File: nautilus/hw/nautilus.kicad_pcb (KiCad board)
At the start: 4 copper layers, 54.7 x 55 mm, 120 parts, among them IC1 DRV8353SRTAR, IC2 STM32G474CEU6, IC3 MAX15062AATA+T, J1 XT30XT30PW_MALE, J2 Conn_01x02_Pin, J3 Conn_01x02_Pin, J4 Conn_01x02_Pin, M1 PAD24AWG_PAD, M2 PAD24AWG_PAD, M3 PAD24AWG_PAD, SW1 SW_Push, U2 CSD88599Q5DCT, U3 CSD88599Q5DCT, U4 AS5147, U5 CSD88599Q5DCT, U7 SN65HVD232

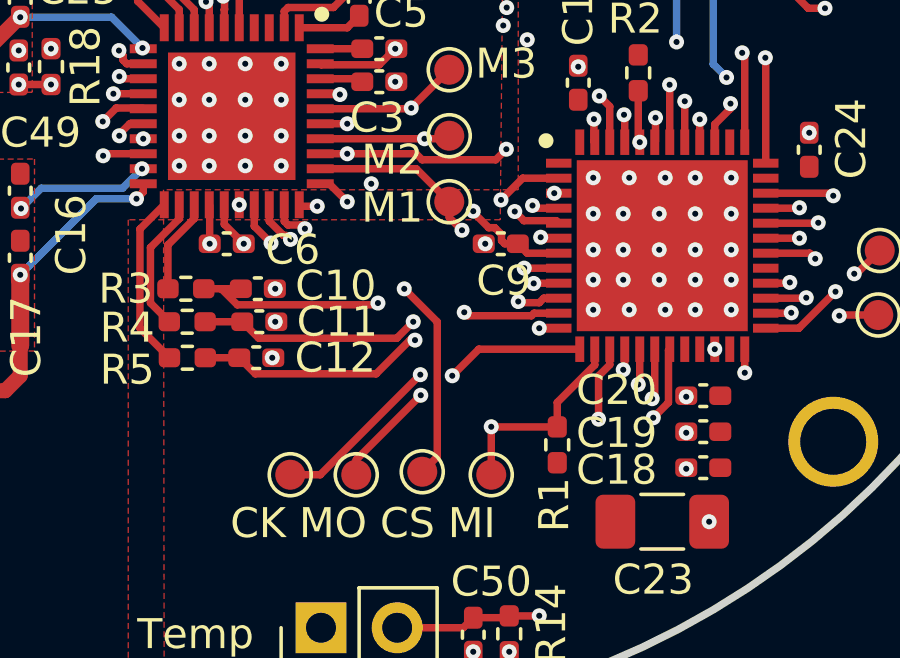
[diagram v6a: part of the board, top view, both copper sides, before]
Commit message: SPI: add temperature reading
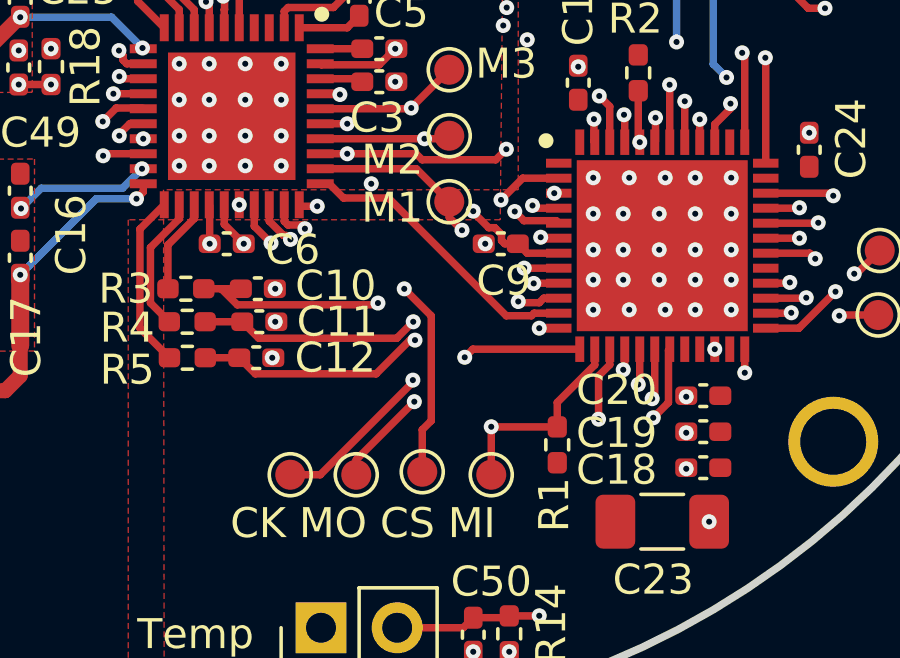
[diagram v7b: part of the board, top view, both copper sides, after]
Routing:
- net /MOTOR_ENABLE: vias 2 -> 0

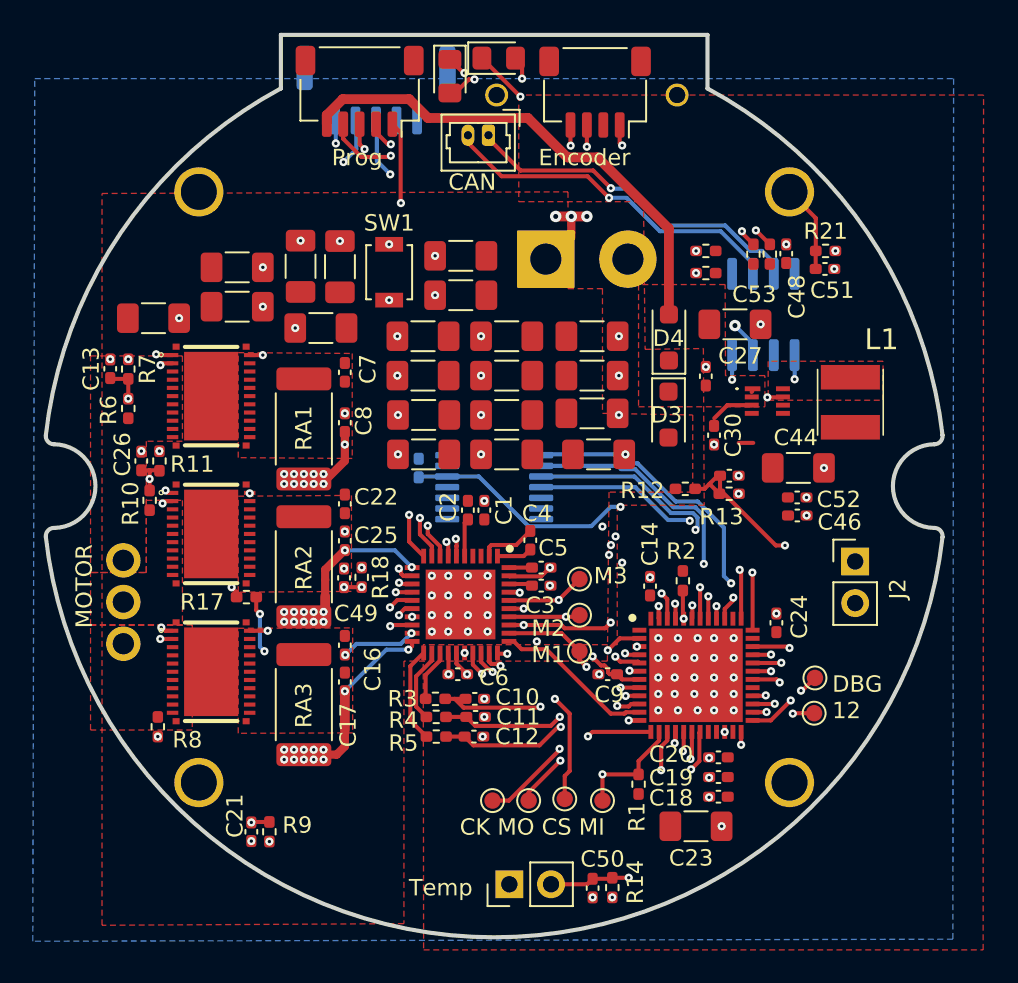
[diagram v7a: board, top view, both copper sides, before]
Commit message: [Hardware] PCB V2: new layout, using LQFP package for microcontroller.
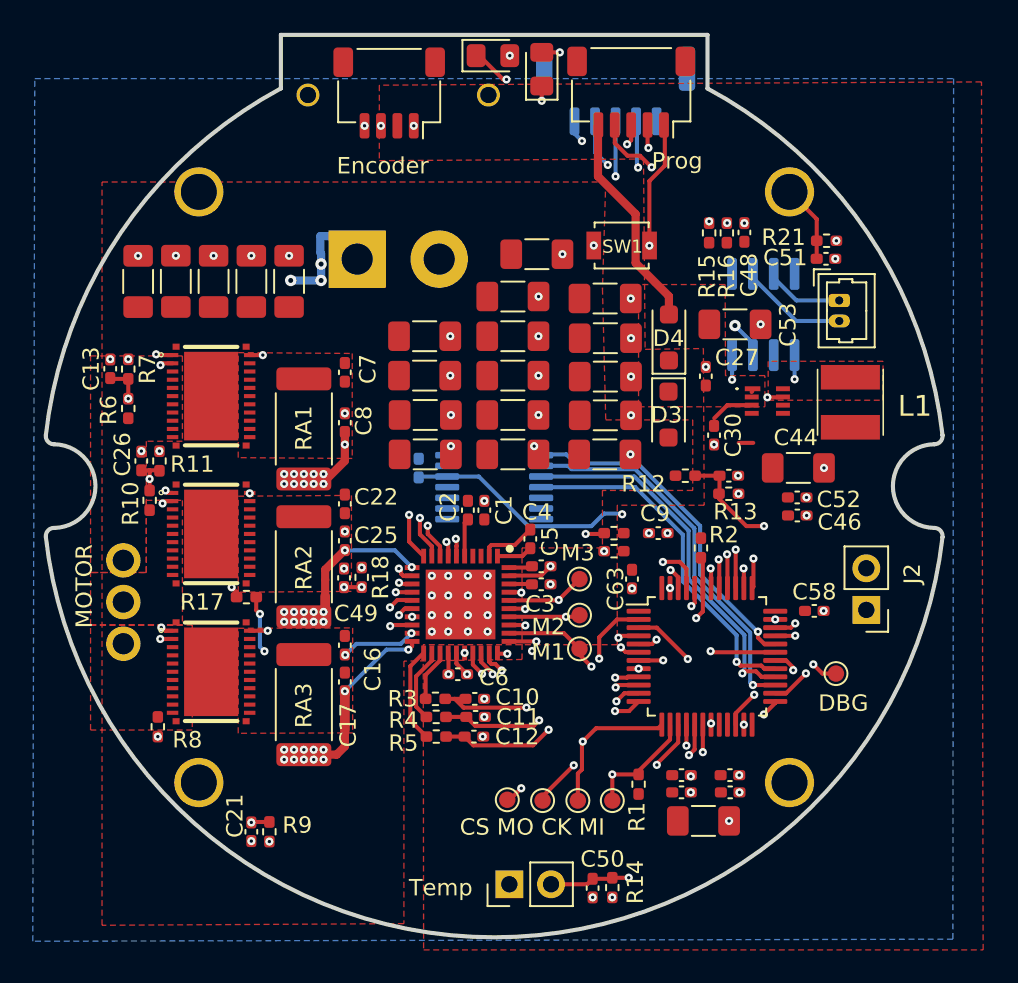
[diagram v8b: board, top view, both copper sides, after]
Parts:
- removed C18: 1uF, Capacitor_SMD:C_0402_1005Metric_Pad0.74x0.62mm_HandSolder
- removed C19, C20, C24: 0.1uF, Capacitor_SMD:C_0402_1005Metric_Pad0.74x0.62mm_HandSolder
- removed C23: 10uF 50V, Capacitor_SMD:C_1206_3216Metric_Pad1.33x1.80mm_HandSolder
- removed DBG2: PAD24AWG_PAD, TestPoint:TestPoint_Pad_D1.0mm
- removed IC2: STM32G474CEU6, nautilus:QFN50P700X700X60-49N-D
- added C58: 0.1uF, Capacitor_SMD:C_0402_1005Metric_Pad0.74x0.62mm_HandSolder, F.Cu at (165.5, 89.9)
- added C59: 1uF, Capacitor_SMD:C_0402_1005Metric_Pad0.74x0.62mm_HandSolder, F.Cu at (160.4, 101.0)
- added C60: 0.1uF, Capacitor_SMD:C_0402_1005Metric_Pad0.74x0.62mm_HandSolder, F.Cu at (157.4, 101.0)
- added C61: 0.1uF, Capacitor_SMD:C_0402_1005Metric_Pad0.74x0.62mm_HandSolder, F.Cu at (157.4, 100.0)
- added C62: 10uF 50V, Capacitor_SMD:C_1206_3216Metric_Pad1.33x1.80mm_HandSolder, F.Cu at (158.8, 102.7)
- added C63: 0.1uF, Capacitor_SMD:C_0402_1005Metric_Pad0.74x0.62mm_HandSolder, F.Cu at (154.4, 88.0)
- added locked: STM32G474CET6, Package_QFP:LQFP-48_7x7mm_P0.5mm, F.Cu at (159.0, 92.7)
- C14: value 0.1uF -> 10nF
- NT4: moved to B.Cu
- R15: value 560 -> 2k
- R16: value 560 -> 1k
- moved J4 23.6 mm to (167.0, 71.0), turned to -90 degrees
- moved R20 19.1 mm to (153.3, 86.3)
- moved R19 16.8 mm to (153.3, 85.2)
- moved DEBUG1 16.6 mm to (154.3, 58.3)
- moved NT4 15.3 mm to (135.4, 67.6), turned to 90 degrees
- moved SPI1 14.6 mm to (153.4, 58.2)
- moved SW1 14.3 mm to (153.8, 67.7), turned to 0 degrees
- moved SPI2 12.6 mm to (139.6, 58.4)
- moved C14 12.5 mm to (160.4, 100.0), turned to 0 degrees
- moved C57 12.0 mm to (148.6, 68.2), turned to 0 degrees
- moved J1 11.5 mm to (137.7, 68.5)
- moved C55 11.5 mm to (124.3, 69.9), turned to 90 degrees
- moved C56 9.18 mm to (152.8, 70.9), turned to 0 degrees
- moved C9 9.14 mm to (156.0, 85.2), turned to 0 degrees
- moved D2 5.62 mm to (148.9, 56.9), turned to 90 degrees
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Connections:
- J2 pad 2: /DEBUG_RX -> GNDS
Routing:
- net /SPI3_CS: track 0.00 -> 30.9 mm, vias 0 -> 2
- net +5V: track 30.3 -> 13.3 mm
- net Net-(J4-Pin_1): track 20.7 -> 4.56 mm, vias 1 -> 0
- net /DEBUG2: track 14.6 -> 0.00 mm, vias 2 -> 0
- net /SWCLK: track 46.4 -> 31.9 mm, vias 3 -> 2
- net /SWDIO: track 45.0 -> 30.9 mm, vias 3 -> 2
- net Net-(J4-Pin_2): track 20.4 -> 6.35 mm, vias 1 -> 0
- net /SPI3_MISO: track 45.3 -> 31.8 mm, vias 3 -> 2
- net /SPI3_SCK: track 45.1 -> 32.9 mm, vias 3 -> 2
- net /SPI3_MOSI: track 41.5 -> 30.9 mm, vias 3 -> 2
- net /DEBUG_RX: track 9.25 -> 0.00 mm, vias 1 -> 0
- net /NRST: track 42.6 -> 35.0 mm
- net /I2C_ABS_SCL: track 34.6 -> 41.7 mm
- net /LED2: track 44.7 -> 37.9 mm
- net /LED1: track 49.1 -> 42.3 mm
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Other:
- board text added: "CS MO CK MI"
- board text added: "DBG"
- board text removed: "CAN"
- board text removed: "CK MO CS MI"
- board text removed: "DBG 12"
